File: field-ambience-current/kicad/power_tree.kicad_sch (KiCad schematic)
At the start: 13 parts, among them J1 USB_C_Receptacle (TYPE-C-31-M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, U5 AP7361C-33 1A LDO (+5V->+3V3,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

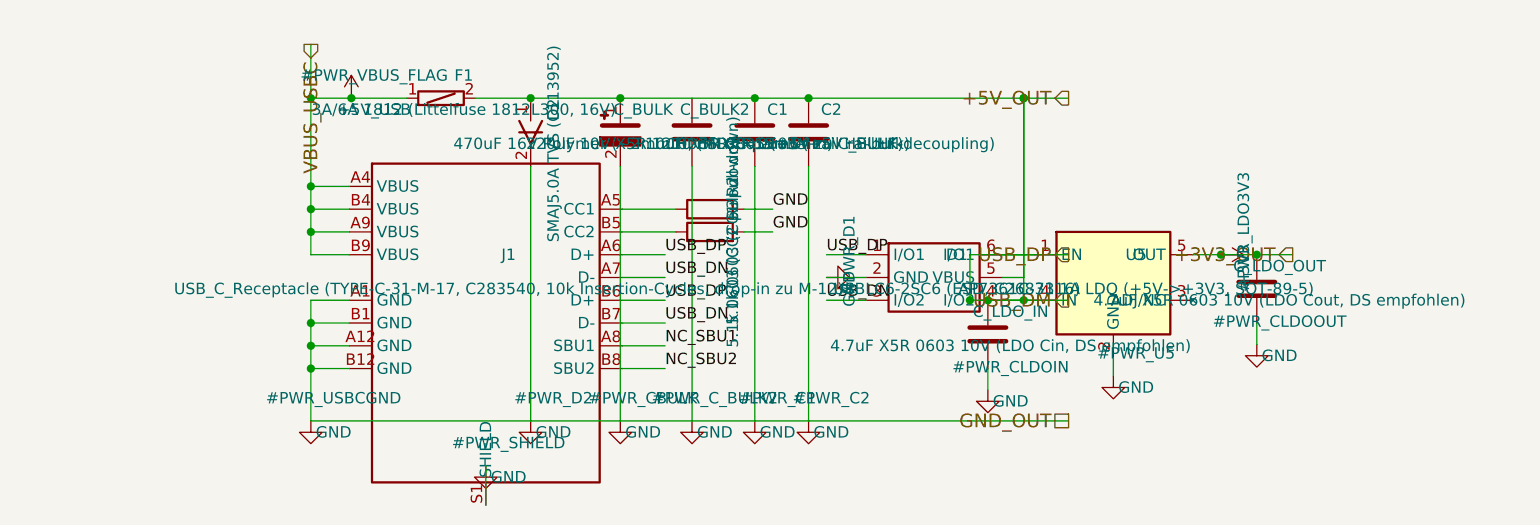
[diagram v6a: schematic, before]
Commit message: pcb(r18.19): Audit-Fixes — USB-C 16-Pin-Revert, Audio-Jack-FP, Speaker-Sync, Regen
Senior-Engineer-Audit deckte vier Defekte auf:

🔴 CRITICAL — USB-C-Stecker-Revert auf 16-Pin M-12
LCSC C283540 (TYPE-C-31-M-17) ist 6-Pin POWER-ONLY (LCSC-Produktseite "6P"):
keine D+/D-, kein CC1/CC2. USB-DFU-Flashen über PA11/PA12 wäre physikalisch
unmöglich gewesen — SW_BOOT-Story aus ADR-0009 wäre kaputt, alle
USB_DM/USB_DP/CC-Pads im Schaltplan floateten. Revert auf C165948
(TYPE-C-31-M-12, 16-Pin volle USB-C-Belegung, 168k+ Stock). Insertion-
Cycle-Trade-Off 10k → ~5k bewusst akzeptiert. Lehre: Pin-Count immer aus
Produktseite verifizieren, nicht aus "drop-in laut Bauform" ableiten.

🟠 HIGH — Audio-Jack-Footprint inkompatibel zum verbauten Teil
J8/J9 hatten Connector_Audio:Jack_3.5mm_CUI_SJ-3523-SMT_Horizontal
zugewiesen. Verbaut wird C431535 (SHOU HAN PJ-320D) mit anderem Pad-Layout
(4 SMD-Pads bei 2.8mm-Pitch + 2 NPTH-Posts). Assembly wäre gescheitert.
EasyEDA-CAD-verifizierter Footprint in Project-Lib vendored als
field_ambience:Jack_3.5mm_PJ-320D_SMT (gleiche Methodik wie SW_TS1088).

🟠 HIGH — Speaker-Wert im Audio-Sheet seit r18.18 stale
J6/J7 hatten value="Speaker L/R (PUI AS04008PS, 4R 4W)" + MPN PUI AS04008.
Drei Fehler: 4Ω (seit r14 als 8Ω korrigiert; Power-Budget rechnet 8Ω),
PUI statt CMS-402811-28SP (r18.18 Primärwahl), Papier-Variante.
Aktualisiert auf "Same Sky CMS-402811-28SP Cloth-Cone 8R 2W".

🟠 CRITICAL (Prozess) — Generator seit r18.14b nicht regeneriert
Alle Entscheidungen r18.15–r18.18 lebten nur in Docs. Schematic (einzige
Netlist-Quelle) hing auf r18.14b. Mit r18.19 erstmals wieder regeneriert.

Verifizierung:
- 8/8 .kicad_sch paren-balanced
- USB-C: 4× C165948/M-12 in power_tree, 0 ungewollte M-17-Leftovers
- Jack-FP: 1× field_ambience:Jack_3.5mm_PJ-320D_SMT in audio, 0 CUI-Leftovers
- Speaker: 6× CMS-402811-28SP, 0 "PUI 4R" Leftovers
- Firmware 13/13 Suiten PASS

Files: generate_kicad_project.py (3 Edits + speaker MPN props),
field_ambience.pretty/Jack_3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
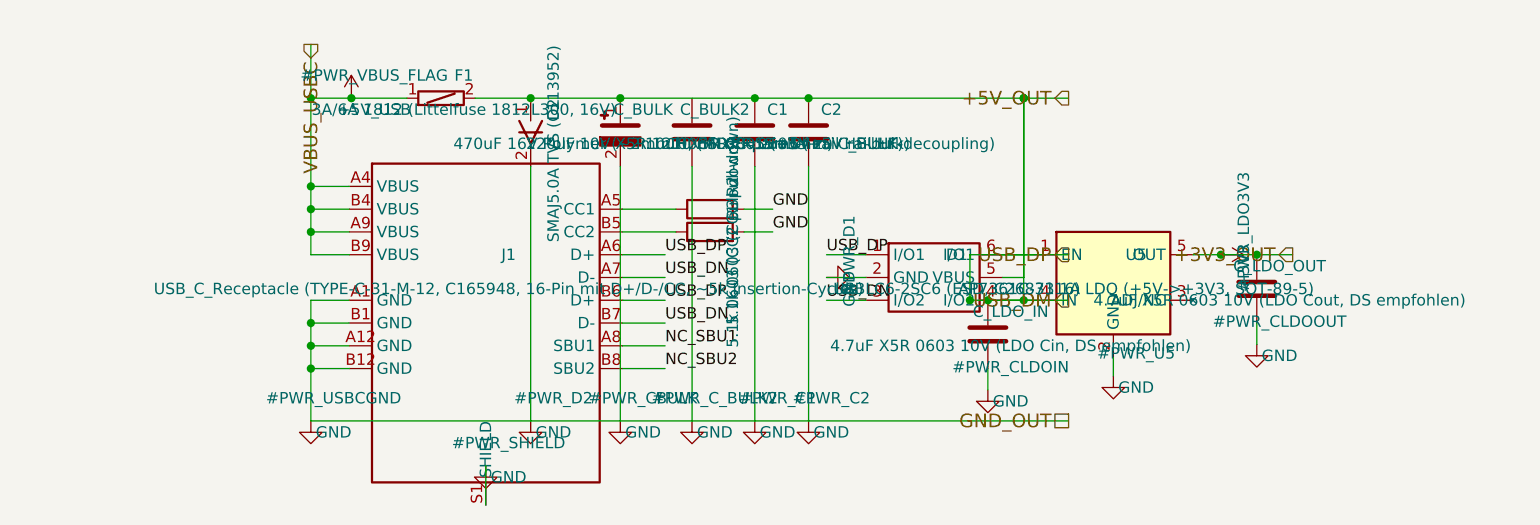
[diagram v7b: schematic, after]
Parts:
- J1: value USB_C_Receptacle (TYPE-C-31-M-17, C283540, 10k Insertion-Cycles, drop-in zu M-12) -> USB_C_Receptacle (TYPE-C-31-M-12, C165948, 16-Pin mit D+/D-/CC, ~5k Insertion-Cycles); LCSC C283540 -> C165948; MPN TYPE-C-31-M-17 -> TYPE-C-31-M-12; Notes r18.10: Upgrade von C165948 (M-12 / 5k Cycles) auf M-17 (10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 -> r18.19-REVERT auf das 16-Pin-Original: Die r18.10/r18.14-Va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
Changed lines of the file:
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@@
       (property "Reference" "J1" (at 52.54 77.46 0)
         (effects (font (size 1.27 1.27))))
-      (property "Value" "USB_C_Receptacle (TYPE-C-31-M-17, C283540, 10k Insertion-Cycles, drop-in zu M-12)" (at 52.54 81.27 0)
+      (property "Value" "USB_C_Receptacle (TYPE-C-31-M-12, C165948, 16-Pin mit D+/D-/CC, ~5k Insertion-Cycles)" (at 52.54 81.27 0)
         (effects (font (size 1.27 1.27))))
       (property "Footprint" "Connector_USB:USB_C_Receptacle_HRO_TYPE-C-31-M-12" (at 50.0 80.0 0)
         (effects (font (size 1.27 1.27)) hide))
-      (property "Datasheet" "https://www.lcsc.com/datasheet/lcsc_datasheet_2108131830_Korean-Hroparts-Elec-TYPE-C-31-M-17_C283540.pdf" (at 50.0 80.0 0)
+      (property "Datasheet" "https://datasheet.lcsc.com/lcsc/1903211732_Korean-Hroparts-Elec-TYPE-C-31-M-12_C165948.pdf" (at 50.0 80.0 0)
         (effects (font (size 1.27 1.27)) hide))
-      (property "MPN" "TYPE-C-31-M-17" (at 52.54 83.81 0)
+      (property "MPN" "TYPE-C-31-M-12" (at 52.54 83.81 0)
         (effects (font (size 1.27 1.27)) hide))
-      (property "LCSC" "C283540" (at 52.54 85.08 0)
+      (property "LCSC" "C165948" (at 52.54 85.08 0)
         (effects (font (size 1.27 1.27)) hide))
-      (property "Notes" "r18.10: Upgrade von C165948 (M-12 / 5k Cycles) auf M-17 (10k Cycles). Footprint M-12 ist drop-in kompatibel (laut HRO-Tabelle); pre-fab in Phase 6 visuell gegen M-17-Drawing prüfen. r18.14: LCSC-Nr. korrigiert — C165935 war ein STF18N65M5-MOSFET (TO-220F-3), via EasyEDA-CAD-Verifikation entdeckt. Korrekt: C283540. 3D-STEP in field_ambience.3dshapes (H=3.2mm)." (at 52.54 86.35 0)
+      (property "Notes" "r18.19-REVERT auf das 16-Pin-Original: Die r18.10/r18.14-Variante C283540 (TYPE-C-31-M-17) wurde am LCSC-Produktseite als **6-Pin POWER-ONLY** identifiziert — keine D+/D-, kein CC. Damit waere USB-DFU-Flashen (PA11/PA12, ADR-0009) physikalisch unmoeglich gewesen und alle USB_DM/USB_DP-/CC-Pads des Schematic floateten. Zurueck auf C165948 (16-Pin volle USB-C-Belegung, 168k+ Stock). Insertion-Cycle-Trade-Off 10k -> ~5k bewusst akzeptiert (typischer Hobby-Gebrauch < 5k ueber Jahre)." (at 52.54 86.35 0)
         (effects (font (size 1.27 1.27)) hide))
     (instances

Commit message: pcb(r18.20b): Sourcing-Fills — alle JLC-bestückbaren TBD-LCSC geschlossen
Sourcing-Agent lieferte verifizierte in-Stock-LCSC für alle r18.20-TBDs:
- C_HSE1/2:  C107045 (Yageo 27pF C0G/NP0 0603, JLC Basic, ~834k Stock)
- C_BULK:    C444831 (Kyocera AVX TPSE477K010R0100, 470µF/10V Polymer Case-E)
- C_BULK2:   C2880380 (Taiyo Yuden 100µF/10V 1210)
- LED gelb:  C2287 (Hubei KENTO KT-0603Y, Vf 2.4V) — Hold + 5 Cell
- LED grün:  C12624 (Hubei KENTO KT-0603G pure-green, Vf 3.1V) — Shift + 5 Cell

Engineering-Flag 1: "220µF/10V/1210 existiert nicht" (220µF nur bis 6.3V im
1210). Statt 220µF/6.3V (am 5V-Rail auf ~70-110µF derated) → 100µF/10V mit
echtem Headroom. Effektiv-Bulk vergleichbar, audit-sauber.

Engineering-Flag 2: <25mΩ-Flach-Polymer (Panasonic SVPF/Kemet T520) bei LCSC
nicht lagernd. Bester JLC-Flach-Polymer C444831 (100mΩ). Verfehlt 10mΩ-Ziel,
aber paralleler 100µF-MLCC (~5mΩ) dominiert Transient-Impedanz → Bulk-ESR
unkritisch. Footprint Case-D→Case-E (7343-43, 4.3mm, passt in 8mm-Top-Zone).

Beifang: BOM_MASTER §9 sagte "220Ω LED-R", Generator sagt 390Ω (an +5V-Anode
→ LED → PCA9685-Sink). 5V/390Ω: gelb 6.7mA, grün 4.9mA — beide im 2-8mA-
Fenster, Wert bleibt. BOM_MASTER korrigiert.

Verifizierung: 8/8 paren-balanced, 0 TBD-VERIFY-Leftovers in power_tree+mcp,
LED gelb ×6 + grün ×6, Firmware 13/13 PASS.

Files: generate_kicad_project.py (5 Fills), 3 Sheets regen, BOM_MASTER,
ADR-0011 (ESR-Realität), CHANGELOG, PROJECT_QUALITY BOM 9.5→10, Readiness 6.5→7.

https://claude.ai/code/session_01K5kLTFpDCCoYwx2dq6RkAv
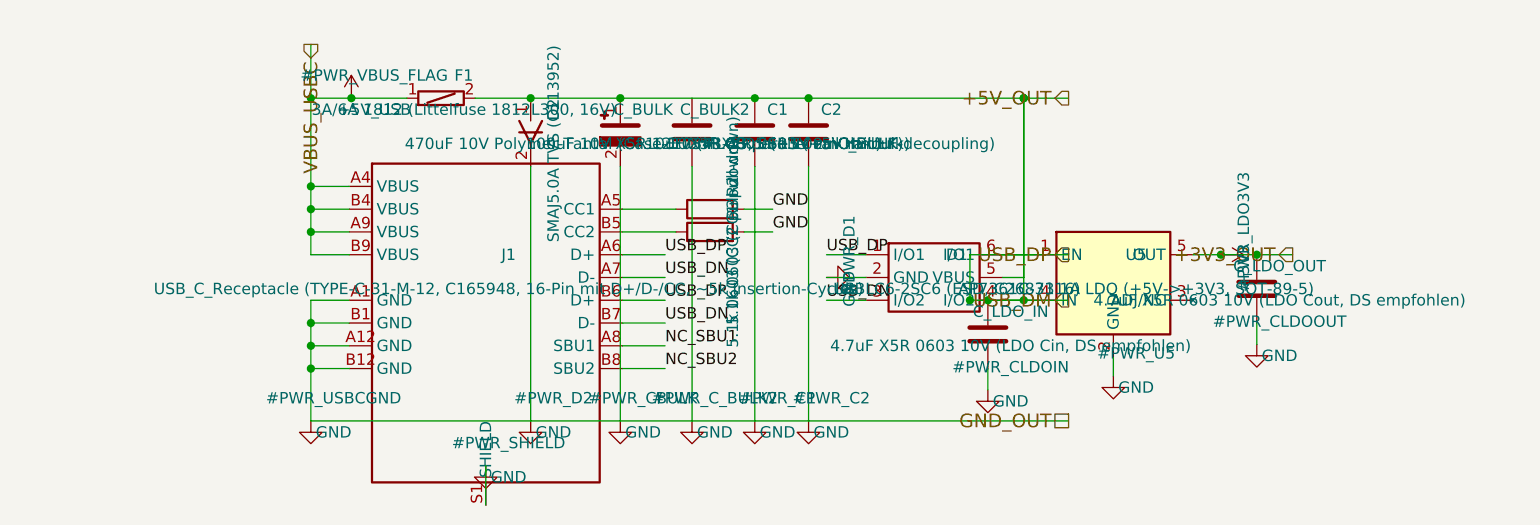
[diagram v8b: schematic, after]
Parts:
- C_BULK: value 470uF 16V Polymer (~2mm H, ESR<=15mOhm) -> 470uF 10V Polymer-Tantal (Case-E 7343-43, ESR 100mOhm); footprint Capacitor_SMD:CP_Tantalum_Case-D_EIA-7343-31_Reflow -> Capacitor_SMD:CP_Tantalum_Case-E_EIA-7343-43_Reflow; LCSC TBD-VERIFY (JLC-Stock vor Layout pruefen) -> C444831; MPN TBD-VERIFY (Panasonic SVPF-Familie oder Kemet T520D Polymer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 -> TPSE477K010R0100 (Kyocera AVX, Polymer-Tantal); Notes r18.12 (ADR-0011): Polymer statt 1000uF Alu — passt in 8mm-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 -> r18.20b: Sourcing final. 470uF/10V Polymer-Tantal Case-E (7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
- C_BULK2: value 220uF 10V X5R 1210 (MLCC parallel zu C_BULK) -> 100uF 10V X5R 1210 (MLCC parallel zu C_BULK); LCSC TBD-VERIFY -> C2880380; MPN TBD-VERIFY (220uF/10V X5R 1210, z.B. CL32A227KQVNNNE) -> LMK325ABJ107MM-T (Taiyo Yuden, 100uF 10V X5R)
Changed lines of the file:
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@@
       (property "Reference" "C_BULK" (at 67.54 61.27 0)
         (effects (font (size 1.27 1.27))))
-      (property "Value" "470uF 16V Polymer (~2mm H, ESR<=15mOhm)" (at 67.54 65.08 0)
+      (property "Value" "470uF 10V Polymer-Tantal (Case-E 7343-43, ESR 100mOhm)" (at 67.54 65.08 0)
         (effects (font (size 1.27 1.27))))
-      (property "Footprint" "Capacitor_SMD:CP_Tantalum_Case-D_EIA-7343-31_Reflow" (at 65 63.81 0)
+      (property "Footprint" "Capacitor_SMD:CP_Tantalum_Case-E_EIA-7343-43_Reflow" (at 65 63.81 0)
         (effects (font (size 1.27 1.27)) hide))
       (property "Datasheet" "~" (at 65 63.81 0)
         (effects (font (size 1.27 1.27)) hide))
-      (property "MPN" "TBD-VERIFY (Panasonic SVPF-Familie oder Kemet T520D Polymer-Tantal 470uF/16V)" (at 67.54 67.62 0)
+      (property "MPN" "TPSE477K010R0100 (Kyocera AVX, Polymer-Tantal)" (at 67.54 67.62 0)
         (effects (font (size 1.27 1.27)) hide))
-      (property "LCSC" "TBD-VERIFY (JLC-Stock vor Layout pruefen)" (at 67.54 68.89 0)
+      (property "LCSC" "C444831" (at 67.54 68.89 0)
         (effects (font (size 1.27 1.27)) hide))
-      (property "Notes" "r18.12 (ADR-0011): Polymer statt 1000uF Alu — passt in 8mm-Top-Zone, besserer ESR. Mit C_BULK2 (220uF MLCC) parallel = ~690uF effective." (at 67.54 70.16 0)
+      (property "Notes" "r18.20b: Sourcing final. 470uF/10V Polymer-Tantal Case-E (7343-43, 4.3mm H — passt in 8mm-Top-Zone), JLC Extended ~517 Stock. ESR 100mOhm (NICHT <25mOhm — die <25mOhm-Flachteile sind bei LCSC nicht lagernd; siehe ADR-0011). Die niedrige Transient-ESR liefert der parallele C_BULK2-MLCC (~5mOhm). 16V/8mOhm-Alternative C403795 (Panasonic 16SEPG470M) waere ein zylindrischer 8x8.9mm-Can mit ~43 Stock — verworfen wegen Bauhoehe + Stock." (at 67.54 70.16 0)
         (effects (font (size 1.27 1.27)) hide))
     (instances
@@
       (property "Reference" "C_BULK2" (at 75.54 61.27 0)
         (effects (font (size 1.27 1.27))))
-      (property "Value" "220uF 10V X5R 1210 (MLCC parallel zu C_BULK)" (at 75.54 65.08 0)
+      (property "Value" "100uF 10V X5R 1210 (MLCC parallel zu C_BULK)" (at 75.54 65.08 0)
         (effects (font (size 1.27 1.27))))
       (property "Footprint" "Capacitor_SMD:C_1210_3225Metric" (at 73 63.81 0)
@@
       (property "Datasheet" "~" (at 73 63.81 0)
         (effects (font (size 1.27 1.27)) hide))
-      (property "MPN" "TBD-VERIFY (220uF/10V X5R 1210, z.B. CL32A227KQVNNNE)" (at 75.54 67.62 0)
+      (property "MPN" "LMK325ABJ107MM-T (Taiyo Yuden, 100uF 10V X5R)" (at 75.54 67.62 0)
         (effects (font (size 1.27 1.27)) hide))
-      (property "LCSC" "TBD-VERIFY" (at 75.54 68.89 0)
+      (property "LCSC" "C2880380" (at 75.54 68.89 0)
         (effects (font (size 1.27 1.27)) hide))
     (instances
